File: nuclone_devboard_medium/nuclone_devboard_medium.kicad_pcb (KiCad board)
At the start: 2 copper layers, 50 x 76.2 mm, 38 parts, among them J1 JTAG_2X05, J2 TYPE-C-31-M-12, J3 nuclone_medium_left, J4 nuclone_medium_right, J5 Conn_02x06_Odd_Even, SW1 RESET, SW2 Bootloader, U1 MCP1702-MB, U2 TPESD0504C6

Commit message: moved RLC parts to different libraries, fixed DRC errors, minor silk movements
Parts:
- added C5: 10n, SquantorCapacitor:C_0402, F.Cu at (84.0, 72.7)
- added R9: 470, SquantorResistor:R_0402_hand, F.Cu at (84.0, 70.5)
- C1, C17, C2: footprint SquantorRcl:C_0603 -> SquantorCapacitor:C_0603
- C14, C4: footprint SquantorRcl:C_0402 -> SquantorCapacitor:C_0402
- C3: value 1u -> 10u; footprint SquantorRcl:C_0402 -> SquantorCapacitor:C_0603
- C9: footprint SquantorRcl:C_0805 -> SquantorCapacitor:C_0805
- F1: footprint SquantorRcl:F_0603_hand -> SquantorFuse:F_0603_hand
- FB1: footprint SquantorRcl:L_0603 -> SquantorInductor:L_0603
- J2: footprint SquantorUsb:USB-C-HRO-31-M-12 -> SquantorUsb:USB-C-HRO-31-M-12_aisler
- R1, R13, R14, R2, R3, R4, R5, R6, R7, R8: footprint SquantorRcl:R_0402_hand -> SquantorResistor:R_0402_hand
- moved C3 17.9 mm to (85.5, 99.0)
- moved U1 4.90 mm to (75.1, 72.8), turned to 0 degrees
- moved C9 3.33 mm to (102.2, 67.8), turned to -90 degrees
- moved C1 1.46 mm to (74.5, 76.1), turned to 180 degrees
- moved R1 1.22 mm to (93.0, 72.9)
- moved C4 1.21 mm to (96.0, 74.2), turned to 180 degrees
- moved C17 1.10 mm to (91.6, 72.5)
- moved FB1 1.10 mm to (90.2, 72.5)
- moved R8 1.08 mm to (84.0, 71.6), turned to 0 degrees
- moved F1 1.00 mm to (88.8, 72.5)
- moved R7 0.99 mm to (98.5, 72.9)
- moved H4 0.90 mm to (63.9, 133.4)
- moved C2 0.90 mm to (87.4, 72.5)
- moved H3 0.90 mm to (106.3, 133.4)
- moved C14 0.50 mm to (80.6, 71.1)
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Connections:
- C4 pad 1: /VUSB -> /VBUS
- J2 pad A6: Net-(J2-DP1) -> /DP
- J2 pad A7: Net-(J2-DN1) -> /DN
- J2 pad B6: Net-(J2-DP1) -> /DP
- J2 pad B7: Net-(J2-DN1) -> /DN
- SW2 pad 2: /Bootloader -> Net-(R9-Pad2)
- U2 pad 5: /VUSB -> /VBUS
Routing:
- net /VBUS: track 34.0 -> 83.0 mm, vias 2 -> 4
- net /VDD: track 83.0 -> 124.8 mm
- net /DP: track 0.00 -> 10.4 mm, vias 0 -> 2
- net /DN: track 0.00 -> 9.62 mm, vias 0 -> 2
- net Net-(J2-DP1): track 6.42 -> 0.00 mm, vias 2 -> 0
- net Net-(J2-DN1): track 5.66 -> 0.00 mm, vias 2 -> 0
- net /VSS: track 22.1 -> 27.1 mm, vias 23 -> 15
- net /RESET: track 28.0 -> 32.9 mm
- net /TCK: track 20.2 -> 25.0 mm, vias 1 -> 2
- net Net-(C17-Pad2): track 16.4 -> 19.6 mm
- net Net-(R9-Pad2): track 0.00 -> 2.90 mm
- net Net-(J2-Shield): track 21.6 -> 19.7 mm
- net /TMS: track 20.3 -> 22.1 mm, vias 1 -> 2
- net Net-(J2-CC2): track 3.42 -> 4.59 mm
- net Net-(J2-CC1): track 3.48 -> 4.52 mm
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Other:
- board text added: "GND"
- board text added: "RESET TCK TMS BOOT"

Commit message: updated all footprints, routed and placed, fixed DRC/ERC
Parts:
- C14, C5: value 10n -> 100n; footprint SquantorCapacitor:C_0402 -> SquantorCapacitor:C_0603
- C4: footprint SquantorCapacitor:C_0402 -> SquantorCapacitor:C_0603
- N2: value 20211121 -> 20240107
- N5: value Nuclone Template 20211121 -> Nuclone Template 20240107
- R1, R14, R2, R3, R4, R5, R6, R7, R8, R9: footprint SquantorResistor:R_0402_hand -> SquantorResistor:R_0603_hand
- R13: value 100 -> 470; footprint SquantorResistor:R_0402_hand -> SquantorResistor:R_0603_hand
- U1: value MCP1702-MB -> MCP1702-3.3V
- moved C14 1.48 mm to (82.0, 71.7), turned to 180 degrees
- moved C5 0.81 mm to (84.8, 73.0)
- moved R13 0.73 mm to (81.9, 70.4), turned to 0 degrees
- moved R8 0.71 mm to (84.7, 71.7)
- moved R9 0.71 mm to (84.7, 70.4)
- moved R1 0.35 mm to (93.0, 72.5)
- moved SW1 0.20 mm to (81.9, 66.4)
- moved SW2 0.20 mm to (85.7, 66.4)
- moved C4 0.15 mm to (96.0, 74.3)
- moved R7 0.10 mm to (98.6, 72.9)
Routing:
- net /VDD: track 124.8 -> 123.8 mm
- net Net-(R13-Pad2): track 1.65 -> 2.50 mm
- net Net-(R9-Pad2): track 2.90 -> 2.19 mm
- net Net-(J2-CC2): track 4.59 -> 3.89 mm
- net /RESET: track 32.9 -> 33.6 mm
- net /VSS: track 27.1 -> 26.8 mm, vias 15 -> 14

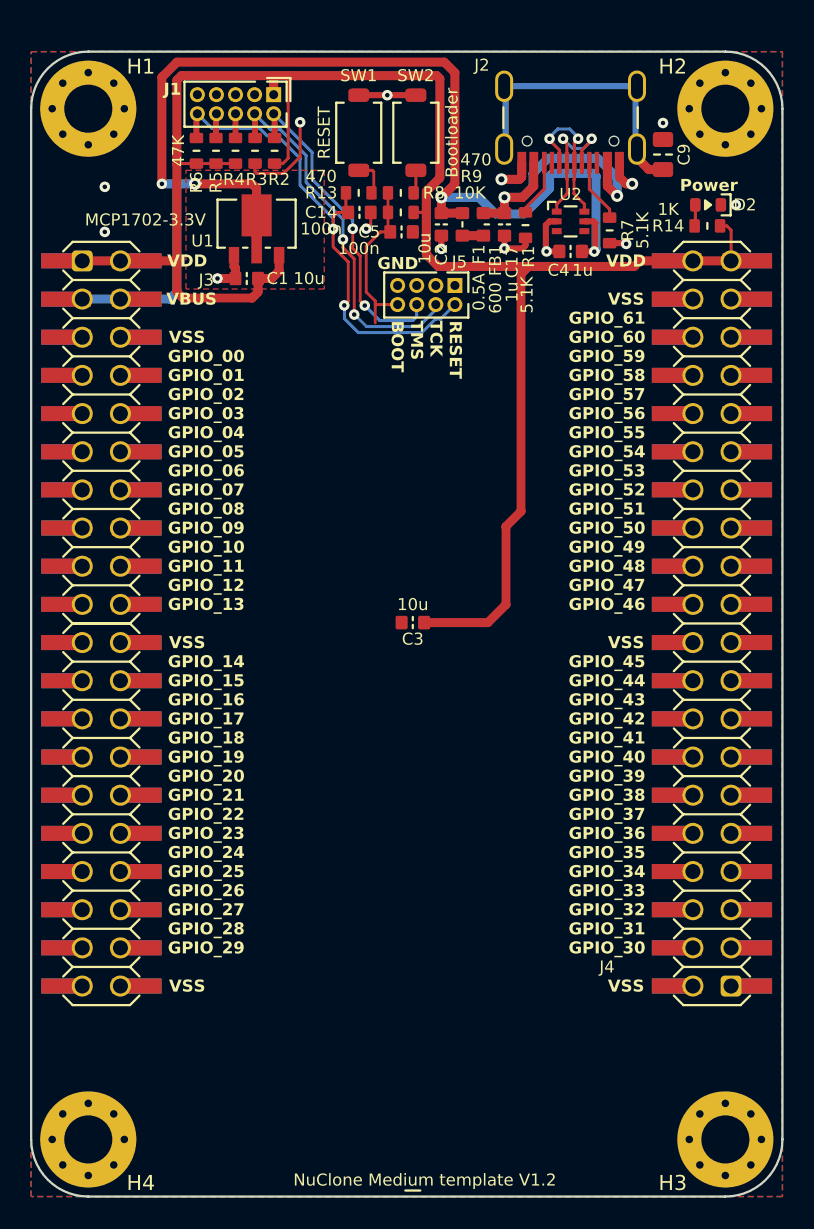
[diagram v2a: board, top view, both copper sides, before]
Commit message: trace optimizations
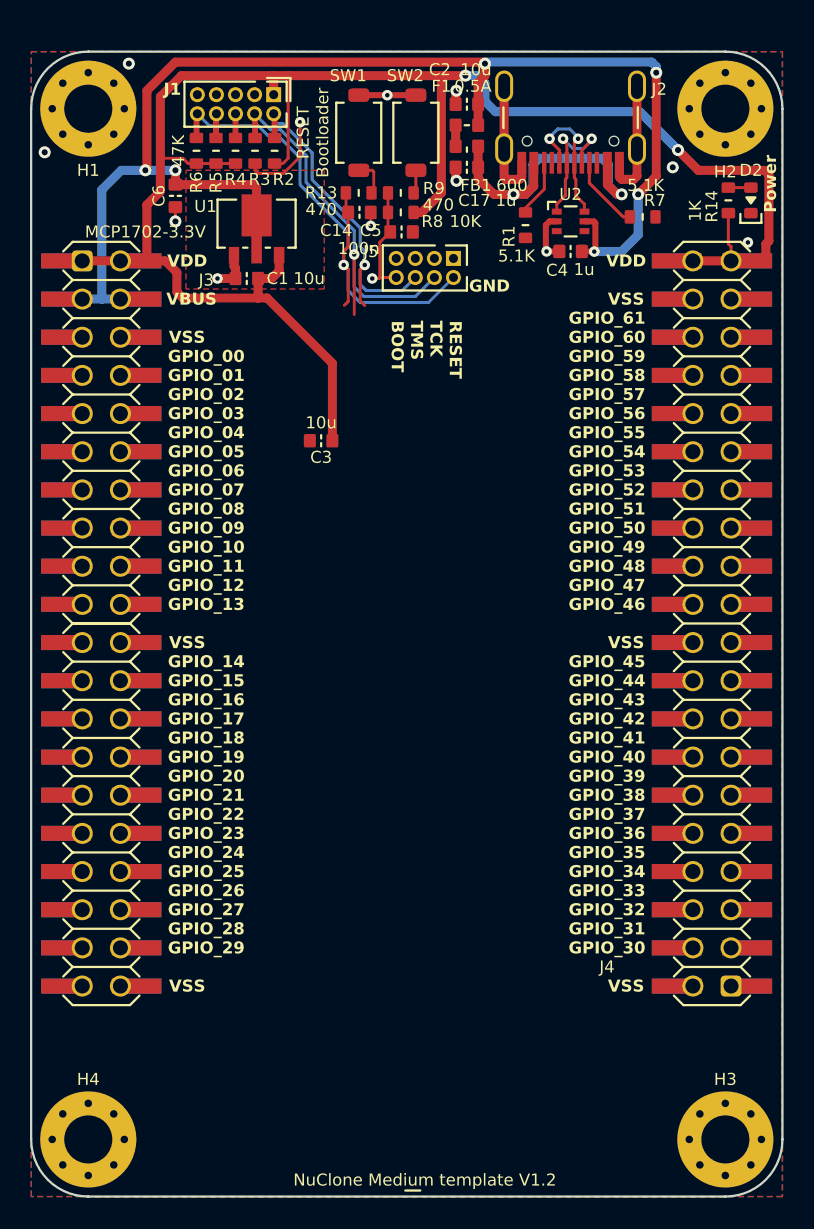
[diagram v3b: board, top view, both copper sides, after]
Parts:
- removed C9: 100n, SquantorCapacitor:C_0805
- added C6: 1u, SquantorCapacitor:C_0603, F.Cu at (69.7, 70.6)
- moved C3 13.6 mm to (79.4, 86.9)
- moved C2 8.18 mm to (89.1, 64.5), turned to 0 degrees
- moved F1 6.61 mm to (89.1, 65.9), turned to 180 degrees
- moved FB1 5.32 mm to (89.1, 67.3), turned to 0 degrees
- moved C17 4.55 mm to (89.1, 68.7), turned to 0 degrees
- moved D2 2.87 mm to (108.0, 70.9), turned to 90 degrees
- moved R7 2.38 mm to (100.8, 72.0), turned to 180 degrees
- moved R14 2.20 mm to (106.5, 70.9), turned to -90 degrees
- moved J5 1.80 mm to (86.3, 75.4)
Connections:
- J2 pad S: Net-(J2-Shield) -> /VSS
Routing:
- net Net-(J2-Shield): track 19.7 -> 0.00 mm
- net /VSS: track 26.8 -> 36.6 mm, vias 14 -> 12
- net /VBUS: track 83.0 -> 88.3 mm, vias 4 -> 6
- net /Bootloader: track 11.5 -> 7.62 mm, vias 0 -> 1
- net /RESET: track 33.6 -> 36.0 mm, vias 2 -> 1
- net Net-(C17-Pad2): track 19.6 -> 21.6 mm
- net /VDD: track 123.8 -> 121.9 mm, vias 0 -> 2
- net /TCK: track 24.7 -> 26.4 mm, vias 2 -> 1
- net /TMS: track 21.7 -> 23.1 mm, vias 2 -> 1
- net Net-(J2-CC1): track 4.21 -> 4.98 mm

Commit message: small modifications
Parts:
- moved SW1 0.60 mm to (81.3, 66.4)
- moved SW2 0.60 mm to (85.1, 66.4)
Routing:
- net /TCK: track 26.4 -> 22.4 mm
- net /TMS: track 23.1 -> 20.2 mm
- net /RESET: track 36.0 -> 33.1 mm

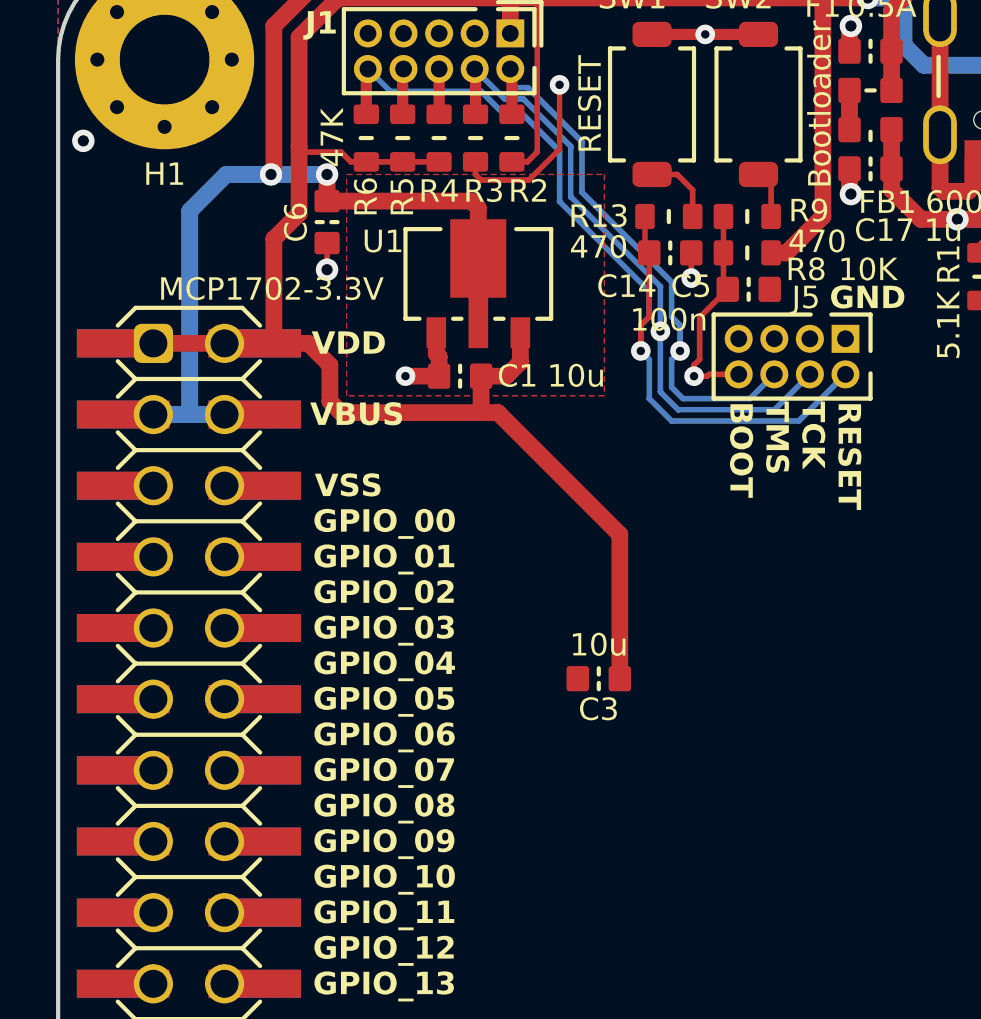
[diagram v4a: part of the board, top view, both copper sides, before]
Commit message: minor silk movements, regulator more cooling
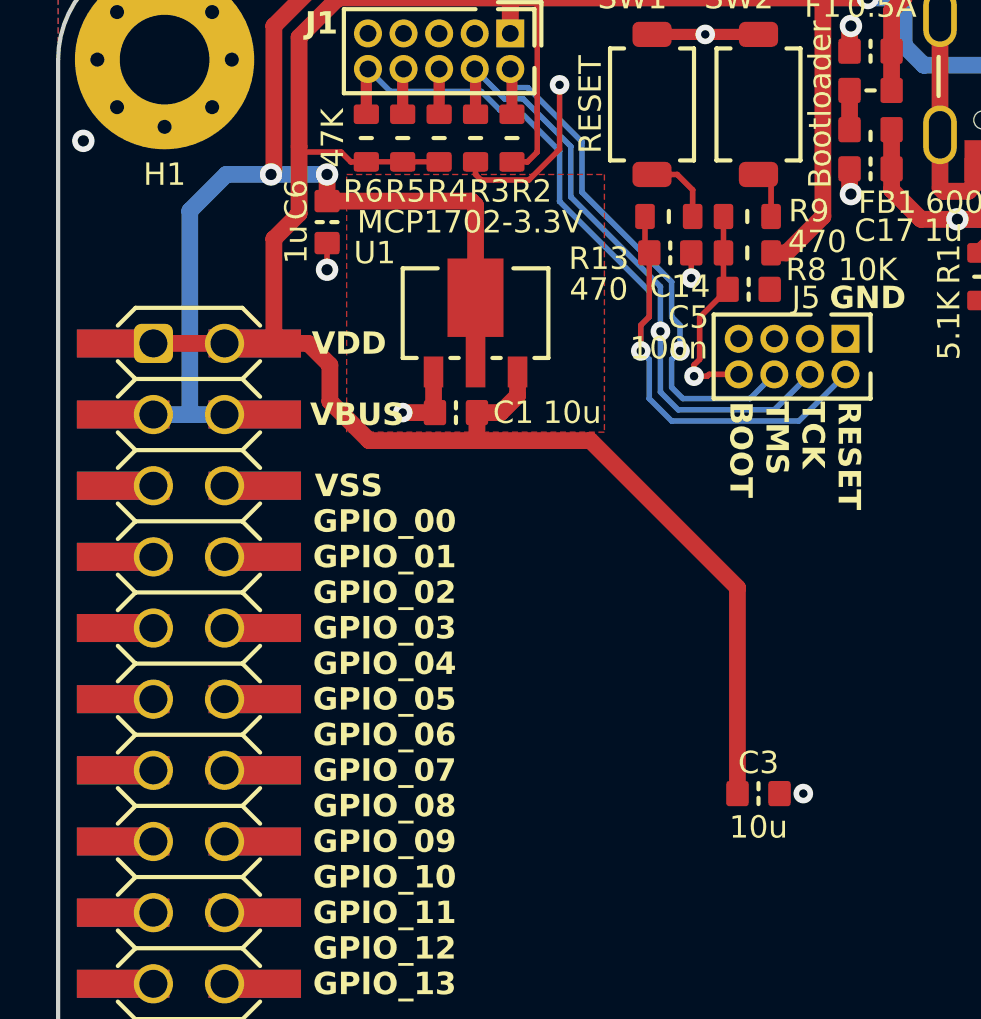
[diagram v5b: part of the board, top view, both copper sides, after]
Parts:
- moved C3 7.02 mm to (85.1, 91.0), turned to 0 degrees
- moved U1 1.40 mm to (75.0, 74.2)
- moved C1 1.31 mm to (74.3, 77.4)
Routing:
- net /VDD: track 121.9 -> 128.7 mm
- net /VBUS: track 88.3 -> 89.4 mm
- net /VSS: track 36.2 -> 36.0 mm, vias 12 -> 13
